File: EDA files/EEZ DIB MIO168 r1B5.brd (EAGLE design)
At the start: 146 x 95 mm, 298 parts, among them IC1 M24C32-WMN6P, IC10 DAC7760IPWPR, IC11 DAC7760IPWPR, IC12 OPA376AIDBVR, IC13 DAC7563TDGSR, IC14 OPA2196IDR, IC15 BTS3408G, IC16 BTS3408G, IC17 BTS3408G, IC18 BTS3408G, IC19 74HC126PW,118, IC2 Si8641BB-B-IS1, IC20 TL431B, IC21 DG468DV-T1-E3, IC22 DG468DV-T1-E3, IC23 DG468DV-T1-E3, IC24 DG468DV-T1-E3, IC25 DG468DV-T1-E3, IC26 DG468DV-T1-E3, IC27 DG468DV-T1-E3, IC28 DG468DV-T1-E3, IC29 DG468DV-T1-E3, IC3 Si8641BB-B-IS1, IC30 DG468DV-T1-E3, IC31 DG468DV-T1-E3, IC32 DG468DV-T1-E3, IC33 DG468DV-T1-E3, IC34 DG468DV-T1-E3, IC35 OPA376AIDBVR, IC36 ADS8674IDBT, IC4 L78L12, IC5 LP2985-50DBVR, IC6 LP2985-33DBVR, IC7 L79L12, IC8 STM32F446ZCT6, IC9 OPA2196IDR, J1 4907, J2 N.C., Q1 2N7002PS,115, Q10 BSS169, Q11 BSS169, Q12 BSS169, Q13 BSS169, Q2 2N7002PS,115, Q3 2N7002PS,115, Q4 2N7002PS,115, Q5 2N7002PS,115, Q6 BSS169, Q7 BSS169, Q8 BSS169, Q9 BSS169, X1 77317-104-28LF, X2 SSW-106-02-S-S, X3 691327310016, X4 691327310016, Y1 25MHz

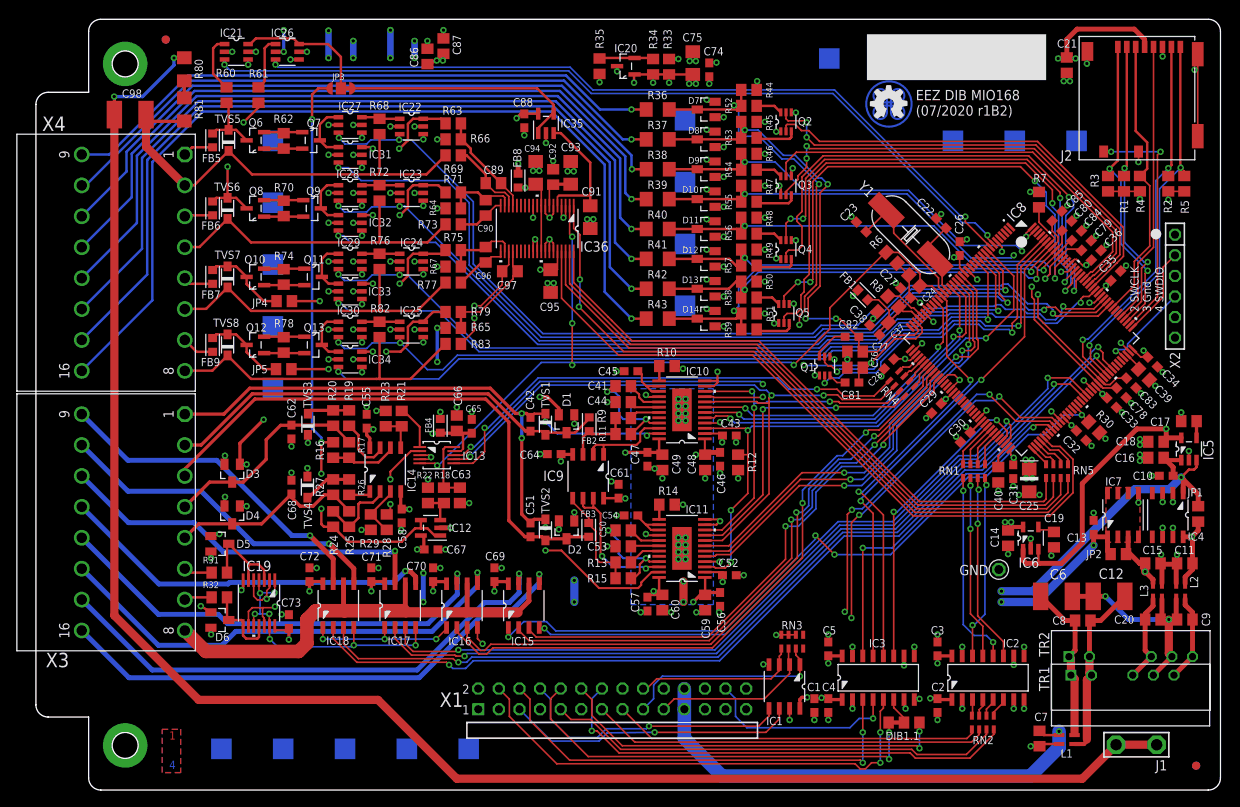
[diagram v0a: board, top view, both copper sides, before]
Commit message: Connectors for piggyback, GND and PWM outputs jumpers
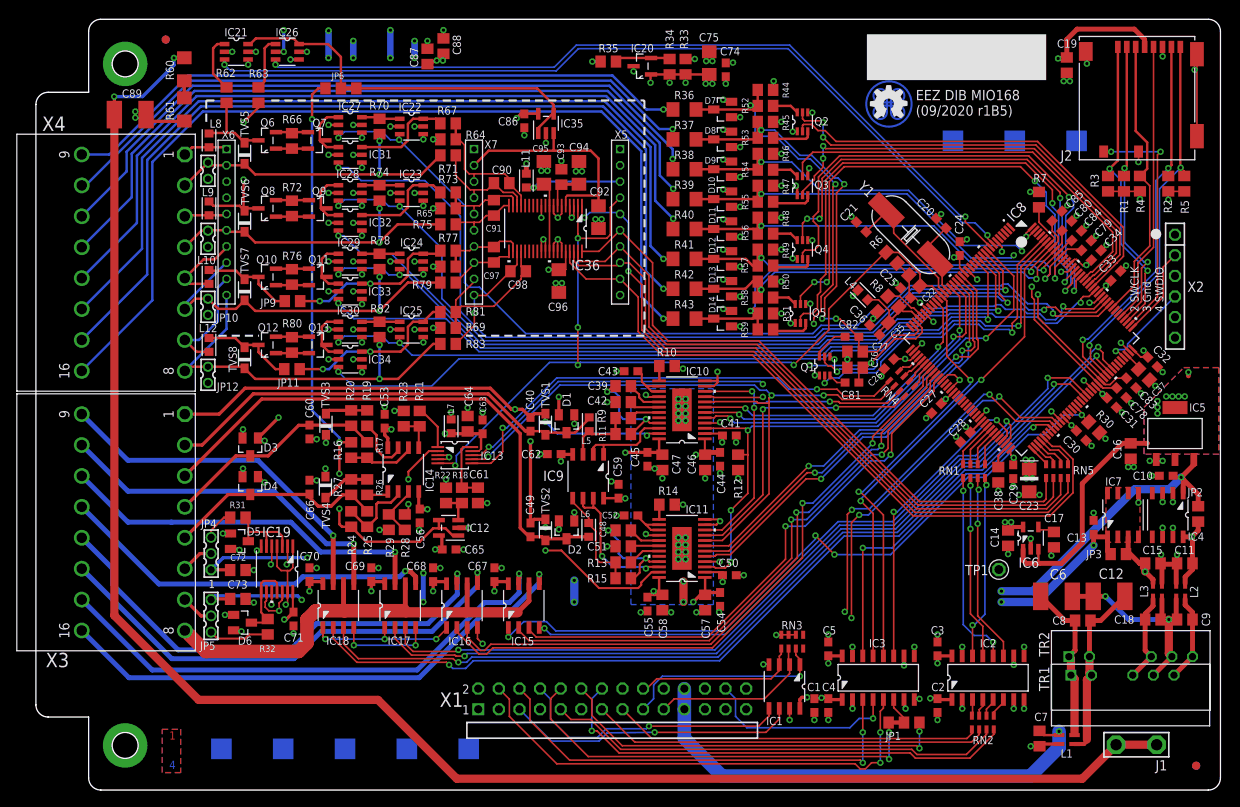
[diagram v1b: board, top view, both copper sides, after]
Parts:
- removed DIB1.1: JP3-CUT-0805-ROTATED, EEZ_Lib1:JP3-0805-CUT2
- removed FB4, FB5, FB6, FB7, FB8, FB9: BLM18AG102SH1D, EEZ_Lib1:BEAD0603
- removed SH5, SH6, SH7, SH8: (no value), EEZ_Lib1:SHORT_NOHOLE
- added JP10, JP12, JP7, JP8: (no value), EEZ_Lib1:2MM-2
- added JP11, JP9: JP2-CUT-0805, EEZ_Lib1:R_0805
- added JP6: JP3-CUT-0805-ROTATED, EEZ_Lib1:JP3-0805-CUT2
- added L10, L11, L12, L7, L8, L9: BLM18AG102SH1D, EEZ_Lib1:BEAD0603
- added X5, X6, X7: 1-2314878-0, EEZ_connectors:1-2314878-0
- C18: value 4u7 -> 1u
- C19: value 10n -> N.C.
- C20: value 1u -> 18p; device rcl:C0805 -> rcl:C0603
- C21: value N.C. -> 18p; device rcl:C0805 -> rcl:C0603
- C22: value 18p -> 1n; device rcl:C0603 -> rcl:C0805
- C23: value 18p -> 4u7; device rcl:C0603 -> EEZ_Lib1:EC1206
- C24: value 1n -> 100n; device rcl:C0805 -> rcl:C0603
- C25: value 4u7 -> 100n; device EEZ_Lib1:EC1206 -> rcl:C0603
- C35, C72, C73, C88: value 100n -> 1u; device rcl:C0603 -> rcl:C0805
- C37: value 1u -> 2u2
- C38: value 100n -> 2u2; device rcl:C0603 -> rcl:C0805
- C39: value 2u2 -> 2n2
- C40: value 2u2 -> 100n; device rcl:C0805 -> rcl:C0603
- C41, C50: value 2n2 -> 100n; device rcl:C0805 -> rcl:C0603
- C42, C51: value 100n -> 22n; device rcl:C0603 -> rcl:C0805
- C44, C53: value 22n -> 100n; device rcl:C0805 -> rcl:C0603
- C46, C47, C57, C58, C64: value 100n -> 4u7; device rcl:C0603 -> rcl:C0805
- C48: value 4u7 -> 2n2
- C49, C59, C60, C66: value 4u7 -> 100n; device rcl:C0805 -> rcl:C0603
- C61: value 100n -> 150n; device rcl:C0603 -> rcl:C0805
- C63: value 150n -> 100n; device rcl:C0805 -> rcl:C0603
- C86: value 1u -> 100n; device rcl:C0805 -> rcl:C0603
- C89: value 2n2 -> 4n7/1kV; device rcl:C0805 -> rcl:C1812
- C90, C97: value 2n2 -> 1n
- C91: value 10u -> 1n; device rcl:C1206 -> rcl:C0805
- C92: value 1u -> 10u; device rcl:C0805 -> rcl:C1206
- C93: value 22u -> 1u; device rcl:C1206 -> rcl:C0805
- C94: value 10u -> 22u
- C96: value 2n2 -> 10u; device rcl:C0805 -> rcl:C1206
- C98: value 4n7/1kV -> 1n; device rcl:C1812 -> rcl:C0805
- IC5: value LP2985-50DBVR -> LM1117MP-5.0; device EEZ_DIB:SOT95P270X145-5N -> EEZ_Lib1:SOT230P696X180-4N
- JP1: value JP2-CUT-0805 -> JP3-CUT-0805-ROTATED; device EEZ_Lib1:R_0805 -> EEZ_Lib1:JP3-0805-CUT2
- JP3: value JP3-CUT -> JP2-CUT-0805; device EEZ_Lib1:JP3-CUT -> EEZ_Lib1:R_0805
- JP4, JP5: value JP2-CUT-0805 -> DS1025-01-1*3P8BV1-B; device EEZ_Lib1:R_0805 -> EEZ_connectors:ZL303-03P
- R60, R61: value 10K -> 560K; device rcl:R0805 -> rcl:R1206
- R62: value 47R -> 10K
- R63: value 1K -> 10K
- R66: value N.C. -> 47R
- R67: value N.C. -> 100R
- R68: value 100R -> N.C.
- R69: value 1K1 -> N.C.
- R70, R74, R78: value 47R -> 100R
- R71, R75, R79: value 1K -> 154R
- R72, R76: value 100R -> 47R
- R73, R77: value 1K1 -> 100R
- R80: value 560K -> 47R; device rcl:R1206 -> rcl:R0805
- R81: value 560K -> 100R; device rcl:R1206 -> rcl:R0805
- R83: value 1K1 -> 154R
- moved JP3 111.7 mm to (133.4, 29.1)
- moved C39 64.2 mm to (72.4, 49.8), turned to 0 degrees
- moved C19 58.5 mm to (127.1, 89.3), turned to 270 degrees
- moved C40 58.0 mm to (61.0, 45.1)
- moved C20 55.4 mm to (111.6, 69.8), turned to 315 degrees
- moved C98 51.6 mm to (59.4, 63.9)
- moved C60 48.3 mm to (33.7, 44.1), turned to 270 degrees
- moved C89 45.6 mm to (11.6, 83.2)
- moved JP1 44.5 mm to (107.0, 8.32), turned to 180 degrees
- moved C55 41.3 mm to (75.4, 22.9), turned to 270 degrees
- moved R81 41.0 mm to (50.8, 58.9), turned to 0 degrees
- moved C56 38.4 mm to (47.3, 33.8)
- moved C23 37.5 mm to (122.4, 38.2), turned to 270 degrees
- moved R80 36.5 mm to (31.6, 54.9), turned to 90 degrees
- moved C58 33.9 mm to (77.2, 23.1), turned to 90 degrees
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- renumbered FB1 to L4, FB2 to L5, FB3 to L6, GND to TP1
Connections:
- removed net N$70: C17.2, IC5.4
- removed net N$90: R76.1, R77.1, SH7.2, TVS7.C1
- new net N$39: JP5.2, X3.7
- new net N$40: JP5.1, R32.1
- new net N$41: JP7.1, R70.1, R71.1, TVS5.C1, X4.2, X6.2
- net !ADC_CS: now also X5.6
- net !RESET: now also C22.1, X5.4; no longer C24.1
- net +12V_ISO: now also C45.1, C47.2, C53.1, C58.2, C59.1, C67.2, C68.2, C72.1, JP2.2, JP4.3; no longer C16.2, C47.1, C49.2, C57.1, C60.2, C61.1, C71.2, C72.2, IC5.1, JP1.2
- net +15V_ISO: now also C87.1, JP2.1; no longer C86.1, JP1.1
- net +3V3_ISO: now also C19.1, C41.1, C50.1, C71.2, C96.2, L7.P$2, X5.10; no longer C21.1, C43.1, C52.1, C73.2, C95.2, FB4.P$2
- net +3V3_MCU: now also C22.2, C23.+, C24.1, C25.1; no longer C24.2, C25.+, C35.1, C36.1
- net +5V_ISO: now also C16.2, IC5.2, IC5.4, L11.P$1, X5.2; no longer C18.2, FB8.P$1, IC5.5
- net -12V_ISO: now also C44.1, C46.2, C54.1, C57.2, C62.1, C73.1, JP3.2, JP5.3, R68.1, R69.1; no longer C46.1, C48.2, C58.1, C59.2, C64.1, JP2.2, R66.1, R67.1
- net -15V_ISO: now also C88.1, JP3.1; no longer C87.1, JP2.1
- net -VSENSE1: now also C40.2; no longer C42.2
- net -VSENSE2: now also C49.2; no longer C51.2
- net 1V25_REF: now also JP6.NO; no longer JP3.NO
- net 2V5_REF: now also C61.2; no longer C63.2
- net ADC_AVDD: now also C86.1, C95.2, L11.P$2, X5.3; no longer C88.1, C94.2, FB8.P$2
- net ADC_IRQ: now also X5.9
- net ADC_MISO: now also X5.8
- net ADC_MOSI: now also X5.5
- net ADC_SCLK: now also X5.7
- net ADC_VREF: now also C92.2, X7.2; no longer C91.2
- net AGND2: now also JP8.1, R74.1, R75.1, X4.4, X6.6; no longer R72.1, R73.1, SH6.2
- net AGND4: now also JP12.1, X4.8, X6.10; no longer SH8.2
- net AIN0: now also L8.P$2, R62.2; no longer FB5.P$2, R60.2
- net AIN1: now also L9.P$2, R63.2; no longer FB6.P$2, R61.2
- net AIN_0GND: now also C90.1, R71.2, X7.4; no longer C89.1, R69.2
- net AIN_0P: now also C90.2, R64.2, R67.2, X7.3; no longer C89.2, R63.2, R66.2
- net AIN_1GND: now also C91.1, R75.2, X7.6; no longer C90.1, R73.2
- net AIN_1P: now also C91.2, R65.2, R73.2, X7.5; no longer C90.2, R64.2, R71.2
- net AIN_2GND: now also C97.1, R79.2, X7.8; no longer C96.1, R77.2
- net AIN_2P: now also C97.2, R68.2, R77.2, X7.7; no longer C96.2, R67.2, R75.2
- net AIN_3GND: now also C98.1, X7.10; no longer C97.1
- net AIN_3P: now also C98.2, R69.2, R81.2, X7.9; no longer C97.2, R65.2, R79.2
- net DAC_OUT#1: now also C40.1; no longer C42.1
- net DAC_OUT#2: now also C49.1; no longer C51.1
- net DIB_CSB: now also JP1.NO; no longer DIB1.1.NO
- net DIB_IRQ: now also JP1.NC; no longer DIB1.1.NC
- net GND: now also C19.2, C20.1, C21.1, C23.-, C24.2, C25.2, C37.1, C38.1, C41.2, C42.1, C44.2, C46.1, C47.1, C50.2, C51.1, C53.2, C57.1, C58.1, C59.2, C60.2, C61.1, C63.2, C64.1, C66.2, C67.1, C68.1, C72.2, C73.2, C89.2, C96.1, IC5.1, JP10.2, JP12.2, JP7.2, JP8.2, R61.2, X5.1, X7.1; no longer C18.1, C19.1, C21.2, C22.1, C23.1, C25.-, C37.2, C38.2, C39.1, C40.1, C44.1, C46.2, C47.2, C48.1, C49.1, C53.1, C57.2, C58.2, C59.1, C60.1, C61.2, C63.1, C64.2, C66.1, C67.2, C68.2, C72.1, C73.1, C91.1, C98.2, IC5.2, R81.2, SH5.1, SH6.1, SH7.1, SH8.1, X4.2, X4.4, X4.6, X4.8
- net HART#1: now also C42.2; no longer C44.2
- net HART#2: now also C51.2; no longer C53.2
- net N$106: now also C17.2; no longer C19.2
- net N$11: now also JP1.COM; no longer DIB1.1.COM
- net N$113: now also C38.2; no longer C40.2
- net N$115: now also C35.1, C36.1; no longer C37.1, C38.1
- net N$126: now also R62.1; no longer R60.1
- net N$130: now also R63.1; no longer R61.1
- net N$136: now also JP9.1, L10.P$2; no longer FB7.P$2, JP4.1
- net N$137: now also JP11.1, L12.P$2; no longer FB9.P$2, JP5.1
- net N$19: now also C48.2; no longer C50.2
- net N$2: now also R80.1; no longer R78.1
- net N$20: now also JP6.COM; no longer JP3.COM
- net N$21: now also R60.2, R61.1; no longer R80.2, R81.1
- net N$22: now also JP4.1; no longer X3.6
- net N$25: now also JP4.2, X3.6; no longer R32.1, X3.7
- net N$26: now also C48.1; no longer C50.1
- net N$28: now also JP11.2, R81.1; no longer JP5.2, R79.1
- net N$3: now also JP10.1, R78.1, R79.1, TVS7.C1, X4.6, X6.8; no longer R68.1, R69.1, SH5.2, TVS5.C1
- net N$31: now also JP6.NC; no longer JP3.NC
- net N$32: now also R72.1; no longer R70.1
- net N$33: now also R72.2; no longer R70.2
- net N$35: now also C94.2; no longer C92.2
- net N$4: now also R80.2; no longer R78.2
- net N$46: now also C52.1; no longer C54.1
- net N$48: now also C18.2; no longer C20.2
- net N$49: now also C18.1; no longer C20.1
- net N$50: now also R74.2; no longer R72.2
- net N$51: now also R73.1; no longer R71.1
- net N$62: now also C39.2; no longer C41.2
- net N$66: now also C43.1; no longer C45.1
- net N$71: now also C63.1, C64.2, L7.P$1; no longer C66.2, C67.1, FB4.P$1
- net N$73: now also C66.1; no longer C68.1
- net N$74: now also C60.1; no longer C62.1
- net N$77: now also R76.1; no longer R74.1
- net N$78: now also R66.1; no longer R62.1
- net N$82: now also C39.1; no longer C41.1
- net N$84: now also R76.2; no longer R74.2
- net N$85: now also R78.2; no longer R76.2
- net N$86: now also R66.2; no longer R62.2
- net N$87: now also JP9.2, R77.1; no longer JP4.2, R75.1
- net N$89: now also R70.2; no longer R68.2
- net N$91: now also L8.P$1, X6.1; no longer FB5.P$1
- net N$92: now also R67.1; no longer R63.1
- net N$93: now also L9.P$1, X6.5; no longer FB6.P$1
- net N$94: now also L10.P$1, X6.7; no longer FB7.P$1
- net N$96: now also L12.P$1, X6.9; no longer FB9.P$1
- net N$97: now also C37.2; no longer C39.2
- net PE: now also C89.1, R60.1; no longer C98.1, R80.1
- net RCC_OSC_IN: now also C20.2; no longer C22.2
- net RCC_OSC_OUT: now also C21.2; no longer C23.2
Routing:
- net N$90: track 40.5 -> 0.00 mm
- net N$41: track 0.00 -> 39.3 mm, vias 0 -> 2
- net ADC_VREF: track 16.5 -> 29.7 mm
- net ADC_AVDD: track 22.9 -> 34.3 mm
- net AGND4: track 40.4 -> 51.1 mm, vias 0 -> 2
- net -12V_ISO: track 248.1 -> 258.7 mm
- net N$96: track 4.04 -> 14.3 mm
- net GND: track 277.9 -> 268.0 mm, vias 176 -> 178
- net !RESET: track 153.6 -> 161.3 mm
- net N$40: track 0.00 -> 7.53 mm
- net N$3: track 40.4 -> 48.0 mm, vias 0 -> 2
- net AIN_3P: track 13.9 -> 20.6 mm
- net N$94: track 3.72 -> 10.1 mm
- net N$119: track 107.4 -> 112.3 mm
- net N$120: track 112.6 -> 117.2 mm
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- added copper zone on layer 1, net +5V_ISO
- added copper zone on layer 16, net +5V_ISO
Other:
- board text added: "EEZ DIB MIO168 (09/2020 r1B5)"
- board text added: "EEZ DIB MIO168 (09/2020 r1B5) Project source code: github.com/eez-open"
- board text removed: "EEZ DIB MIO168 (07/2020 r1B2)"
- board text removed: "EEZ DIB MIO168 (07/2020 r1B2) Project source code: github.com/eez-open"

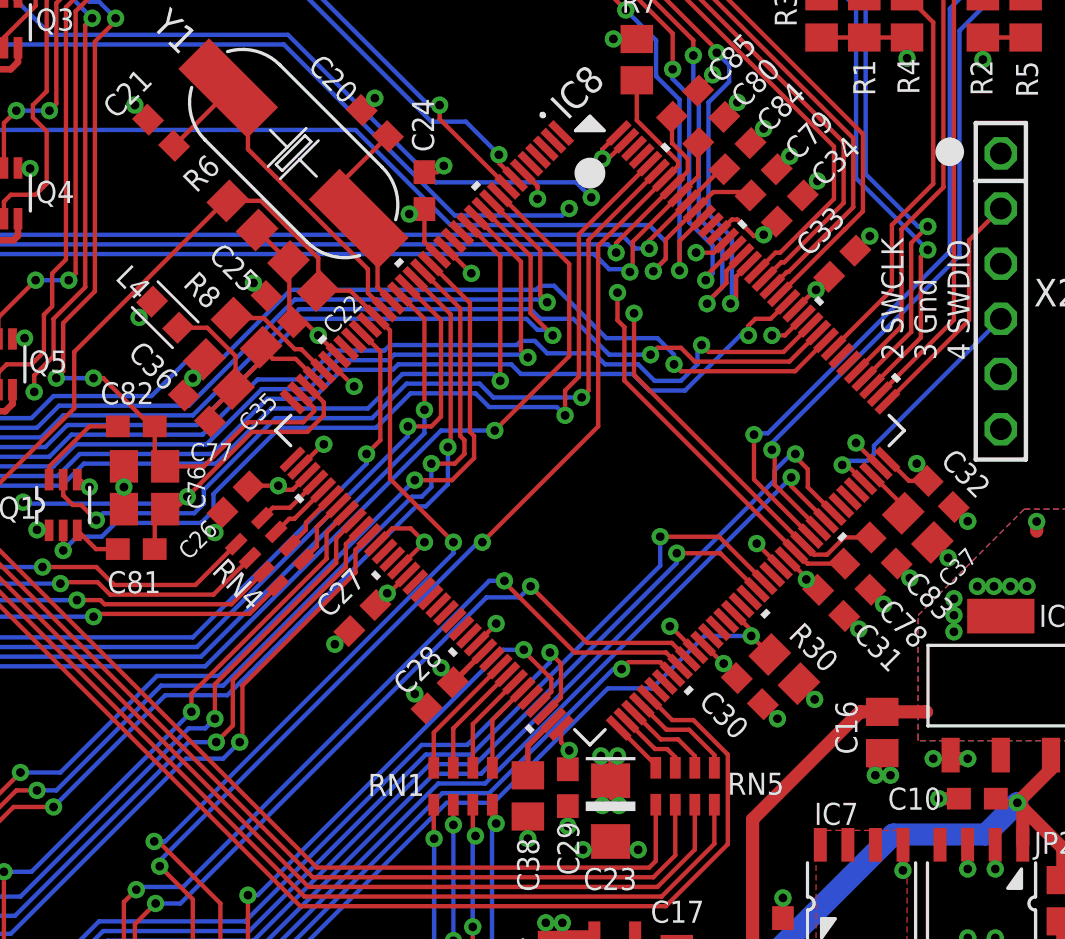
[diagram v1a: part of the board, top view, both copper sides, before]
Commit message: MCU Vdd update
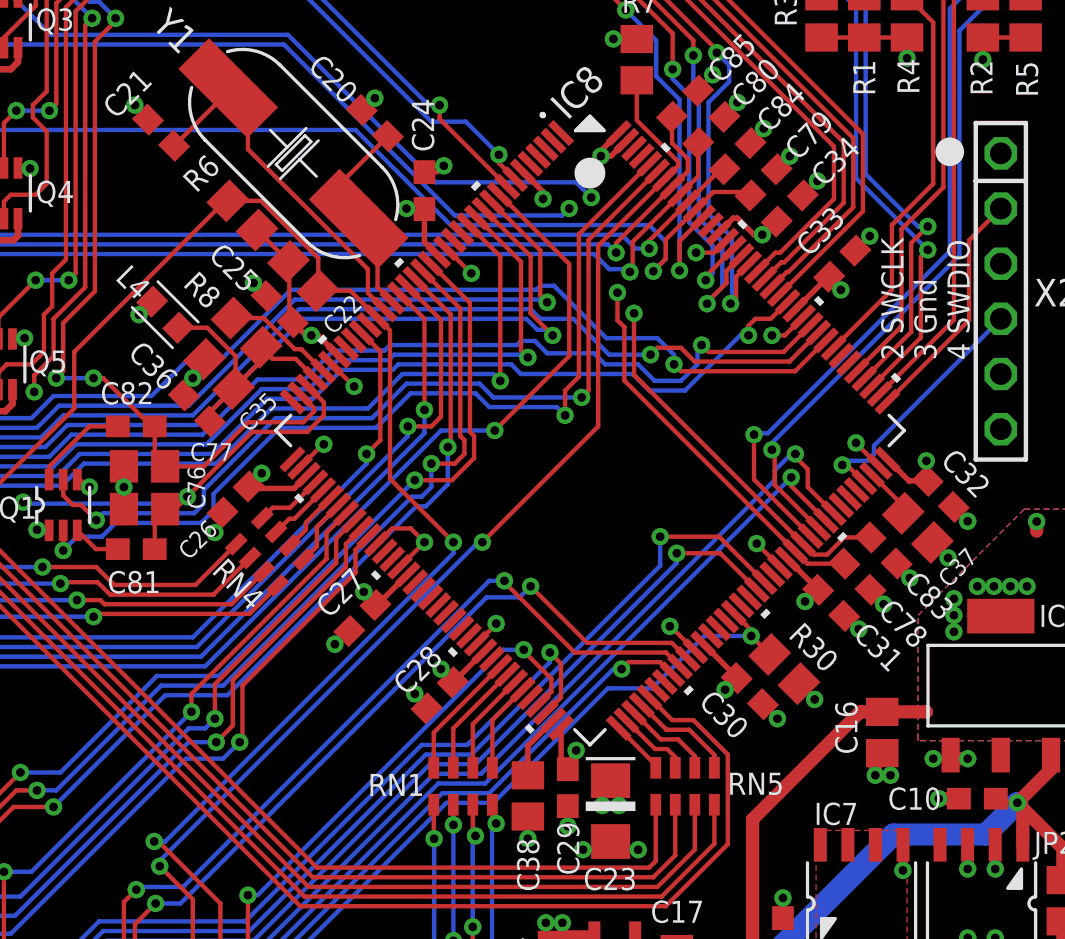
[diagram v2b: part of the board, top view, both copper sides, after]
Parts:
- removed SH1: (no value), EEZ_Lib1:SHORT_NOHOLE
- C22: value 1n -> N.C.
- JP10, JP12, JP7, JP8: value (none) -> DS1025-01-1*2P8BV1-B
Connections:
- removed net +3V3_MCU: C22.2, C23.+, C24.1, C25.1, C26.1, C27.1, C28.1, C29.1, C30.1, C31.1, C32.1, C33.1, C34.1, IC8.108, IC8.121, IC8.131, IC8.143, IC8.144, IC8.17, IC8.30, IC8.39, IC8.52, IC8.6, IC8.62, IC8.72, IC8.84, IC8.95, L4.P$1, R6.1, SH1.1
- net +3V3_ISO: now also C22.2, C23.+, C24.1, C25.1, C26.1, C27.1, C28.1, C29.1, C30.1, C31.1, C32.1, C33.1, C34.1, IC8.108, IC8.121, IC8.131, IC8.143, IC8.144, IC8.17, IC8.30, IC8.39, IC8.52, IC8.6, IC8.62, IC8.72, IC8.84, IC8.95, L4.P$1, R6.1; no longer SH1.2
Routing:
- net +3V3_ISO: track 53.6 -> 98.6 mm, vias 19 -> 33
- net +3V3_MCU: track 42.3 -> 0.00 mm, vias 16 -> 0
- removed copper zone on layer 15, net +3V3_MCU

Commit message: #4, BOM update
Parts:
- removed SH3: (no value), EEZ_Lib1:SHORT_NOHOLE
- C40, C49, C60, C66: value 100n -> 1n; device rcl:C0603 -> rcl:C0805
- moved C49 40.8 mm to (21.3, 41.8)
- moved SH2 40.7 mm to (18.4, 46.5), turned to 180 degrees
- moved C40 39.6 mm to (21.3, 46.2)
- moved C60 14.1 mm to (21.3, 37.4), turned to 90 degrees
- moved C66 13.2 mm to (21.3, 32.9)
- moved R31 3.19 mm to (24.6, 30.4)
- moved D5 3.19 mm to (24.8, 27.5)
- moved JP4 3.19 mm to (21.3, 26.0)
- moved C72 3.11 mm to (24.8, 24.0)
- moved JP5 2.62 mm to (21.3, 18.9)
- moved TVS4 2.22 mm to (35.8, 39.6)
- moved D3 1.59 mm to (28.0, 42.3)
- moved D4 1.59 mm to (28.0, 37.5)
- moved C73 1.53 mm to (24.8, 22.0)
- moved D6 1.40 mm to (25.4, 19.2)
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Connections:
- removed net -VSENSE1: C40.2, IC10.23, SH2.2, TVS1.C1
- removed net -VSENSE2: C49.2, IC11.23, SH3.2, TVS2.C1
- new net -VSENSE: IC10.23, IC11.23, SH2.2
- net GND: now also C40.2, C49.2, TVS1.C1, TVS2.C1; no longer SH3.1
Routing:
- net -VSENSE: track 0.00 -> 140.5 mm, vias 0 -> 4
- net GND: track 268.0 -> 228.3 mm, vias 178 -> 182
- net -VSENSE2: track 37.6 -> 0.00 mm, vias 4 -> 0
- net -VSENSE1: track 20.1 -> 0.00 mm, vias 2 -> 0
- net +3V3_ISO: track 98.6 -> 103.3 mm, vias 33 -> 35
- net N$1: track 69.2 -> 73.5 mm
- net -12V_ISO: track 258.7 -> 260.8 mm
- net N$40: track 7.53 -> 9.45 mm
- net +12V_ISO: track 264.3 -> 262.5 mm
- net N$39: track 4.07 -> 5.85 mm
- net DAC_OUT#2: track 67.9 -> 66.3 mm
- net POUT4: track 59.8 -> 61.4 mm
- net POUT5: track 60.1 -> 61.6 mm
- net N$73: track 27.0 -> 25.6 mm
- net POUT7: track 65.9 -> 67.2 mm
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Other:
- board text added: "EEZ DIB MIO168 (10/2020 r1B5)"
- board text added: "EEZ DIB MIO168 (10/2020 r1B5) Project source code: github.com/eez-open"
- board text removed: "EEZ DIB MIO168 (09/2020 r1B5)"
- board text removed: "EEZ DIB MIO168 (09/2020 r1B5) Project source code: github.com/eez-open"
